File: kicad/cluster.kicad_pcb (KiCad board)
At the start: 2 copper layers, 24.5 x 36.5 mm, 17 parts, among them J1 Conn_01x07

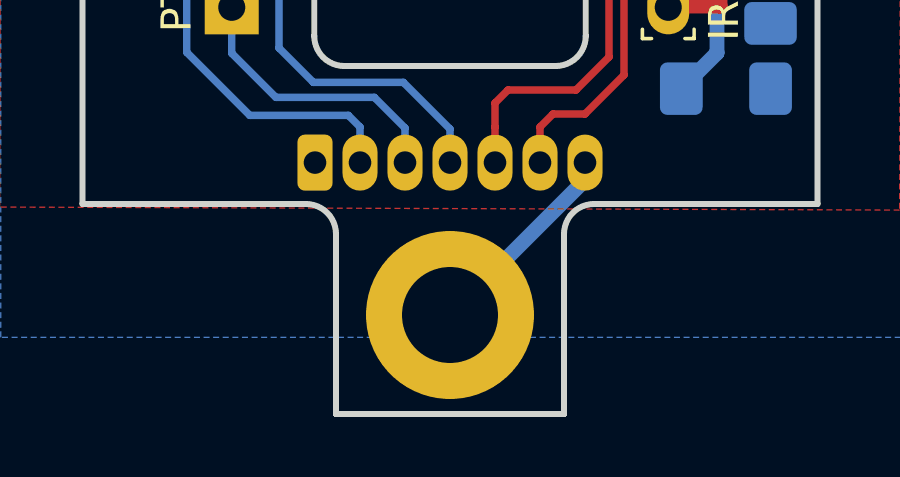
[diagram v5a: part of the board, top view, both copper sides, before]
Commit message: Update the various sensitivity-related resistor values
This updates the transimpedance amplifier resistors to 2k, and adjusts
the LED drive resistors to an appropriate level, from empirical testing.
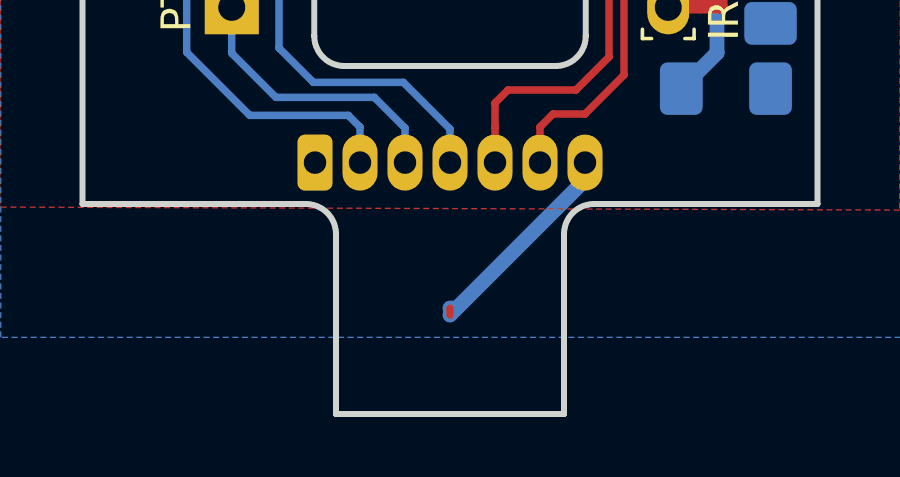
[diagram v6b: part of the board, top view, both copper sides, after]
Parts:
- removed REF**: MountingHole_3.2mm_M3, MountingHole:MountingHole_3.2mm_M3_DIN965_Pad
- R1, R2, R3, R4, R5: value 150 -> 270
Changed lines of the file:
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@@
     (tracks 76)
     (zones 0)
-    (modules 17)
+    (modules 16)
     (nets 13)
   )
@@
   (layers
     (0 F.Cu signal)
-    (31 B.Cu signal)
+    (31 B.Cu signal hide)
     (34 B.Paste user hide)
-    (35 F.Paste user hide)
-    (36 B.SilkS user)
+    (35 F.Paste user)
+    (36 B.SilkS user hide)
     (37 F.SilkS user)
     (38 B.Mask user hide)
-    (39 F.Mask user hide)
-    (40 Dwgs.User user)
+    (39 F.Mask user)
+    (40 Dwgs.User user hide)
     (44 Edge.Cuts user)
     (45 Margin user hide)
     (46 B.CrtYd user hide)
-    (47 F.CrtYd user hide)
-    (48 B.Fab user)
+    (47 F.CrtYd user)
+    (48 B.Fab user hide)
     (49 F.Fab user)
   )
@@
       (effects (font (size 1 1) (thickness 0.15)) (justify mirror))
     )
-    (fp_text value 150 (at 0 -1.82) (layer B.Fab)
+    (fp_text value 270 (at -3.9475 0.035) (layer B.SilkS)
       (effects (font (size 1 1) (thickness 0.15)) (justify mirror))
     )
@@
     )
   )
-  (module MountingHole:MountingHole_3.2mm_M3_DIN965_Pad (layer F.Cu)
-    (at 162.45 96.5)
-    (descr "Mounting Hole 3.2mm, M3, DIN965")
-    (tags "mounting hole 3.2mm m3 din965")
-    (attr virtual)
-    (fp_text reference REF** (at 0 -3.8) (layer F.SilkS) hide
-      (effects (font (size 1 1) (thickness 0.15)))
-    )
-    (fp_text value MountingHole_3.2mm_M3 (at 0 4.2) (layer F.Fab)
-      (effects (font (size 1 1) (thickness 0.15)))
-    )
-    (fp_circle (center 0 0) (end 2.8 0) (layer Cmts.User) (width 0.15))
-    (fp_circle (center 0 0) (end 3.05 0) (layer F.CrtYd) (width 0.05))
-    (pad 1 thru_hole circle (at 0 0) (size 5.6 5.6) (drill 3.2) (layers *.Cu *.Mask)
-      (net 12 GND))
-  )
   (module lalboard:IR908-7C-F (layer F.Cu)
     (at 156.425 67.395 90)
@@
       (effects (font (size 1 1) (thickness 0.15)) (justify mirror))
     )
-    (fp_text value 150 (at 0 -1.82 270) (layer B.Fab)
-      (effects (font (size 1 1) (thickness 0.15)) (justify mirror))
+    (fp_text value 270 (at 0 1.655 270) (layer B.SilkS)
+      (effects (font (size 0.75 0.75) (thickness 0.125)) (justify mirror))
     )
     (fp_line (start -1.6 -0.8) (end -1.6 0.8) (layer B.Fab) (width 0.1))
@@
       (effects (font (size 1 1) (thickness 0.15)) (justify mirror))
     )
-    (fp_text value 150 (at 0 -1.82 270) (layer B.Fab)
-      (effects (font (size 1 1) (thickness 0.15)) (justify mirror))
+    (fp_text value 270 (at 0 -1.649999 270) (layer B.SilkS)
+      (effects (font (size 0.75 0.75) (thickness 0.125)) (justify mirror))
     )
     (fp_line (start -1.6 -0.8) (end -1.6 0.8) (layer B.Fab) (width 0.1))
@@
       (effects (font (size 1 1) (thickness 0.15)) (justify mirror))
     )
-    (fp_text value 150 (at 0 -1.82 180) (layer B.Fab)
+    (fp_text value 270 (at 0 -1.82 180) (layer B.SilkS)
       (effects (font (size 1 1) (thickness 0.15)) (justify mirror))
     )
@@
       (effects (font (size 1 1) (thickness 0.15)) (justify mirror))
     )
-    (fp_text value 150 (at 0 -1.82 270) (layer B.Fab)
+    (fp_text value 270 (at 0 -1.735 270) (layer B.SilkS)
       (effects (font (size 1 1) (thickness 0.15)) (justify mirror))
     )
@@
   (segment (start 170.275 81.245) (end 170.605 81.575) (width 0.5) (layer F.Cu) (net 1))
   (via (at 164.875008 81.245) (size 0.8) (drill 0.4) (layers F.Cu B.Cu) (net 1))
+  (segment (start 157.849999 71.22) (end 157.849999 73.3) (width 0.35) (layer B.Cu) (net 2))
+  (segment (start 154.829999 68.2) (end 157.849999 71.22) (width 0.35) (layer B.Cu) (net 2))
+  (segment (start 153.08 68.2) (end 154.829999 68.2) (width 0.35) (layer B.Cu) (net 2))
+  (segment (start 151.755 69.525) (end 153.08 68.2) (width 0.35) (layer B.Cu) (net 2))
+  (segment (start 171.35 84.400001) (end 171.35 87.765) (width 0.5) (layer B.Cu) (net 3))
+  (segment (start 169.725 83.705) (end 170.654999 83.705) (width 0.5) (layer B.Cu) (net 3))
+  (segment (start 170.654999 83.705) (end 171.35 84.400001) (width 0.5) (layer B.Cu) (net 3))
+  (segment (start 171.35 87.765) (end 170.16 88.955) (width 0.5) (layer B.Cu) (net 3))
+  (segment (start 167.855 78.085) (end 168.475 78.705) (width 0.25) (layer B.Cu) (net 4))
+  (segment (start 167.855 76.3825) (end 167.855 78.085) (width 0.5) (layer B.Cu) (net 4))
+  (segment (start 156.425 67.395) (end 158.965 69.935) (width 0.5) (layer B.Cu) (net 5))
+  (segment (start 173.135 81.585) (end 173.145 81.575) (width 0.25) (layer B.Cu) (net 6))
+  (segment (start 173.135 83.805) (end 173.135 81.585) (width 0.5) (layer B.Cu) (net 6))
   (segment (start 154.295 81.575) (end 153.675 82.195) (width 0.25) (layer B.Cu) (net 7))
   (segment (start 155.775 89.845) (end 159.06 89.845) (width 0.25) (layer B.Cu) (net 7))
@@
   (segment (start 153.675 87.745) (end 155.775 89.845) (width 0.25) (layer B.Cu) (net 7))
   (segment (start 153.739999 82.130001) (end 154.295 81.575) (width 0.25) (layer F.Cu) (net 7))
-  (segment (start 157.895 88.745) (end 160.895 88.745) (width 0.25) (layer B.Cu) (net 10))
-  (segment (start 156.425 81.975) (end 156.75 82.3) (width 0.25) (layer B.Cu) (net 10))
-  (segment (start 156.75 82.3) (end 156.75 87.6) (width 0.25) (layer B.Cu) (net 10))
-  (segment (start 156.425 81.245) (end 156.425 81.975) (width 0.25) (layer F.Cu) (net 10))
-  (segment (start 162.45 90.3) (end 162.45 91.42) (width 0.25) (layer B.Cu) (net 10))
-  (segment (start 160.895 88.745) (end 162.45 90.3) (width 0.25) (layer B.Cu) (net 10))
-  (segment (start 156.75 87.6) (end 157.895 88.745) (width 0.25) (layer B.Cu) (net 10))
+  (segment (start 156.645 89.245) (end 159.9275 89.245) (width 0.25) (layer B.Cu) (net 8))
+  (segment (start 155.175 86.245) (end 155.175 87.775) (width 0.25) (layer B.Cu) (net 8))
+  (segment (start 160.95 90.2675) (end 160.95 91.42) (width 0.25) (layer B.Cu) (net 8))
+  (segment (start 155.175 87.775) (end 156.645 89.245) (width 0.25) (layer B.Cu) (net 8))
+  (segment (start 159.9275 89.245) (end 160.95 90.2675) (width 0.25) (layer B.Cu) (net 8))
   (segment (start 166.65 89) (end 164.384998 89) (width 0.25) (layer F.Cu) (net 9))
   (segment (start 166.25 71.47) (end 166.25 80.426998) (width 0.25) (layer F.Cu) (net 9))
@@
   (segment (start 167.75 87.9) (end 166.65 89) (width 0.25) (layer F.Cu) (net 9))
   (segment (start 167.75 83.5) (end 167.75 87.9) (width 0.25) (layer F.Cu) (net 9))
+  (segment (start 157.895 88.745) (end 160.895 88.745) (width 0.25) (layer B.Cu) (net 10))
+  (segment (start 156.425 81.975) (end 156.75 82.3) (width 0.25) (layer B.Cu) (net 10))
+  (segment (start 156.75 82.3) (end 156.75 87.6) (width 0.25) (layer B.Cu) (net 10))
+  (segment (start 156.425 81.245) (end 156.425 81.975) (width 0.25) (layer F.Cu) (net 10))
+  (segment (start 162.45 90.3) (end 162.45 91.42) (width 0.25) (layer B.Cu) (net 10))
+  (segment (start 160.895 88.745) (end 162.45 90.3) (width 0.25) (layer B.Cu) (net 10))
+  (segment (start 156.75 87.6) (end 157.895 88.745) (width 0.25) (layer B.Cu) (net 10))
   (segment (start 168.25 83.25) (end 168.25 88.5) (width 0.25) (layer F.Cu) (net 11))
   (segment (start 170.605 69.525) (end 169.455 69.525) (width 0.25) (layer F.Cu) (net 11))
@@
   (segment (start 162.45 96.27) (end 162.45 96.5) (width 0.25) (layer F.Cu) (net 12))
   (segment (start 166.95 91.77) (end 166.95 91.87) (width 0.5) (layer B.Cu) (net 12))
-  (segment (start 157.849999 71.22) (end 157.849999 73.3) (width 0.35) (layer B.Cu) (net 2))
-  (segment (start 154.829999 68.2) (end 157.849999 71.22) (width 0.35) (layer B.Cu) (net 2))
-  (segment (start 153.08 68.2) (end 154.829999 68.2) (width 0.35) (layer B.Cu) (net 2))
-  (segment (start 151.755 69.525) (end 153.08 68.2) (width 0.35) (layer B.Cu) (net 2))
-  (segment (start 171.35 84.400001) (end 171.35 87.765) (width 0.5) (layer B.Cu) (net 3))
-  (segment (start 169.725 83.705) (end 170.654999 83.705) (width 0.5) (layer B.Cu) (net 3))
-  (segment (start 170.654999 83.705) (end 171.35 84.400001) (width 0.5) (layer B.Cu) (net 3))
-  (segment (start 171.35 87.765) (end 170.16 88.955) (width 0.5) (layer B.Cu) (net 3))
-  (segment (start 167.855 78.085) (end 168.475 78.705) (width 0.25) (layer B.Cu) (net 4))
-  (segment (start 167.855 76.3825) (end 167.855 78.085) (width 0.5) (layer B.Cu) (net 4))
-  (segment (start 156.425 67.395) (end 158.965 69.935) (width 0.5) (layer B.Cu) (net 5))
-  (segment (start 173.135 81.585) (end 173.145 81.575) (width 0.25) (layer B.Cu) (net 6))
-  (segment (start 173.135 83.805) (end 173.135 81.585) (width 0.5) (layer B.Cu) (net 6))
-  (segment (start 156.645 89.245) (end 159.9275 89.245) (width 0.25) (layer B.Cu) (net 8))
-  (segment (start 155.175 86.245) (end 155.175 87.775) (width 0.25) (layer B.Cu) (net 8))
-  (segment (start 160.95 90.2675) (end 160.95 91.42) (width 0.25) (layer B.Cu) (net 8))
-  (segment (start 155.175 87.775) (end 156.645 89.245) (width 0.25) (layer B.Cu) (net 8))
-  (segment (start 159.9275 89.245) (end 160.95 90.2675) (width 0.25) (layer B.Cu) (net 8))
   (segment (start 166.95 92) (end 162.45 96.5) (width 0.5) (layer B.Cu) (net 12))
   (segment (start 166.95 91.42) (end 166.95 92) (width 0.25) (layer B.Cu) (net 12))

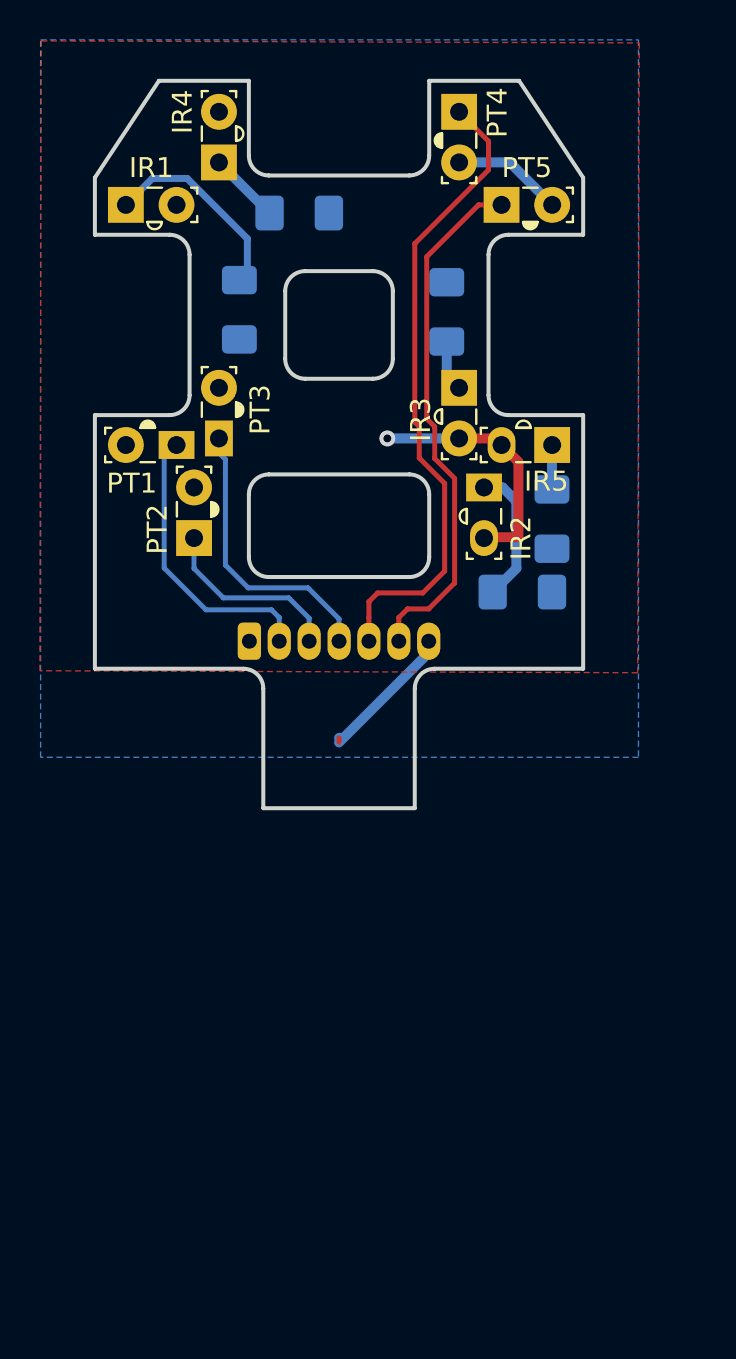
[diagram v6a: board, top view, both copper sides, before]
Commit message: Update cluster pcb for v2.5
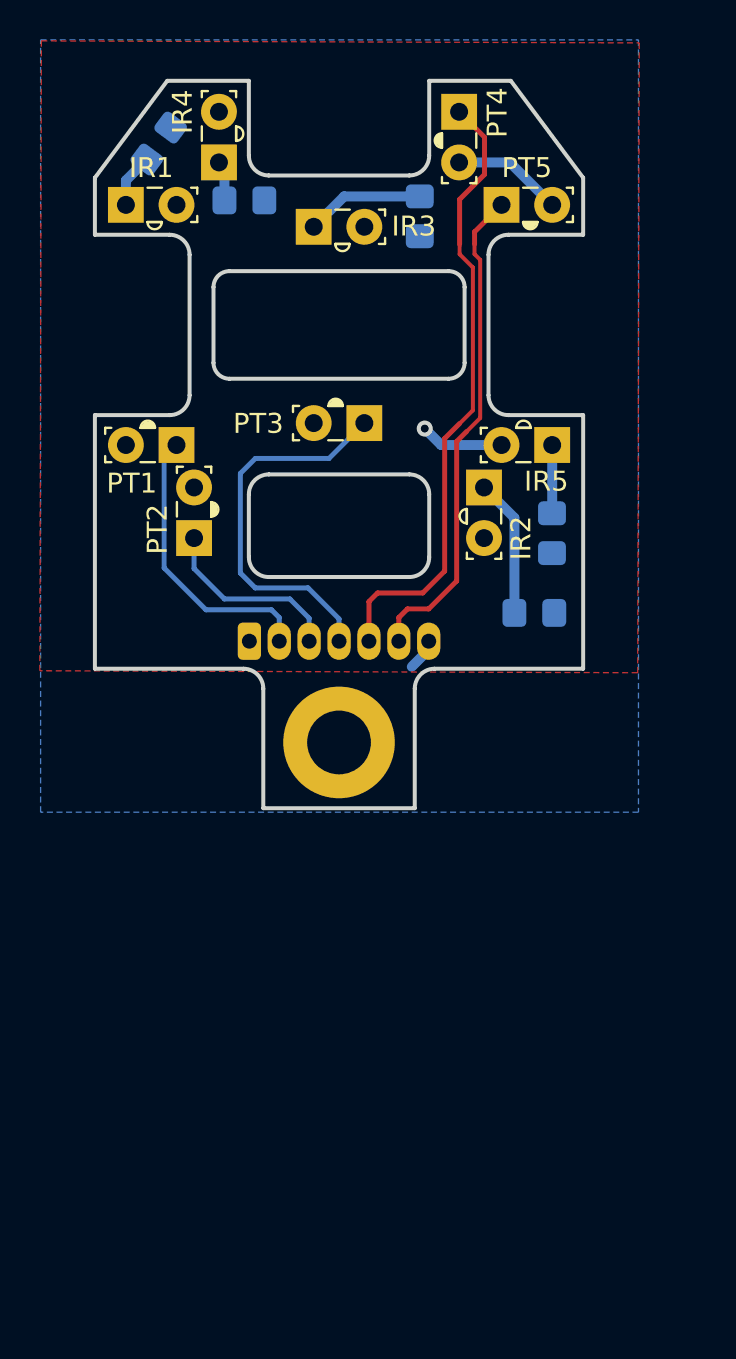
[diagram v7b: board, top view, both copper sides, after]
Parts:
- added H1: MountingHole_Pad, MountingHole:MountingHole_3.2mm_M3_DIN965_Pad, F.Cu at (162.4, 96.5)
- R1, R2, R3, R4, R5: footprint Resistor_SMD:R_1206_3216Metric_Pad1.42x1.75mm_HandSolder -> Resistor_SMD:R_0805_2012Metric_Pad1.20x1.40mm_HandSolder
- moved IR3 10.9 mm to (161.2, 70.6), turned to 0 degrees
- moved R1 9.27 mm to (153.4, 66.4), turned to -126.7 degrees
- moved PT3 7.34 mm to (163.7, 80.5), turned to 180 degrees
- moved R3 4.98 mm to (166.5, 70.1), turned to 90 degrees
- moved R4 2.82 mm to (157.7, 69.3)
- moved R2 1.21 mm to (172.2, 90.0)
- moved R5 0.71 mm to (173.1, 86.0)
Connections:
- net +5V renamed +3.3V
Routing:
- net +3.3V: track 18.4 -> 10.1 mm
- net Net-(IR1-K): track 9.97 -> 2.71 mm
- net GND: track 7.76 -> 2.31 mm
- net C3: track 14.4 -> 19.3 mm
- net Net-(IR3-K): track 2.58 -> 5.95 mm
- net C5: track 26.5 -> 24.9 mm
- net Net-(IR5-K): track 2.23 -> 3.43 mm
- net C4: track 32.2 -> 31.4 mm
- net C1: track 15.2 -> 14.4 mm
- net Net-(IR4-K): track 3.59 -> 2.83 mm
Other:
- outline, holes or cut-outs redrawn
- net class Default removed
- net class Power removed
- board text added: "lalboard.com finger cluster"
- board text added: "v2.5.0"
- board text removed: "Min internal corner radius: .8mm (for all internal corners)"
- board text removed: "finger cluster v0.1"
- board text removed: "lalboard.com"

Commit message: Add production files for the PCBs
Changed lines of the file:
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@@
     (grid_origin 150 100)
     (pcbplotparams
-      (layerselection 0x00210f0_ffffffff)
+      (layerselection 0x00010f0_ffffffff)
       (plot_on_all_layers_selection 0x0000000_00000000)
       (disableapertmacros false)
-      (usegerberextensions false)
-      (usegerberattributes true)
-      (usegerberadvancedattributes true)
-      (creategerberjobfile true)
+      (usegerberextensions true)
+      (usegerberattributes false)
+      (usegerberadvancedattributes false)
+      (creategerberjobfile false)
       (dashed_line_dash_ratio 12.000000)
       (dashed_line_gap_ratio 3.000000)
@@
       (psa4output false)
       (plotreference true)
-      (plotvalue true)
+      (plotvalue false)
       (plotinvisibletext false)
       (sketchpadsonfab false)
-      (subtractmaskfromsilk false)
+      (subtractmaskfromsilk true)
       (outputformat 1)
       (mirror false)
       (drillshape 0)
       (scaleselection 1)
-      (outputdirectory "/tmp/cluster/")
+      (outputdirectory "/home/jesusfreke/projects/lalboard/kicad/production_files/cluster")
     )
   )
@@
     (fp_line (start 1 0.625) (end 1 -0.625)
       (stroke (width 0.1) (type solid)) (layer "B.Fab"))
-    (pad "1" smd roundrect (at -1 0 90) (size 1.2 1.4) (layers "B.Cu" "B.Paste" "B.Mask") (roundrect_rratio 0.208333)
+    (pad "1" smd roundrect (at -1 0 90) (size 1.2 1.4) (layers "B.Cu" "B.Paste" "B.Mask") (roundrect_rratio 0.2083333333)
       (net 12 "GND") (pintype "passive"))
-    (pad "2" smd roundrect (at 1 0 90) (size 1.2 1.4) (layers "B.Cu" "B.Paste" "B.Mask") (roundrect_rratio 0.208333)
+    (pad "2" smd roundrect (at 1 0 90) (size 1.2 1.4) (layers "B.Cu" "B.Paste" "B.Mask") (roundrect_rratio 0.2083333333)
       (net 6 "Net-(IR5-K)") (pintype "passive"))
     (model "${KICAD6_3DMODEL_DIR}/Resistor_SMD.3dshapes/R_0805_2012Metric.wrl"
@@
     (fp_line (start 1 0.625) (end 1 -0.625)
       (stroke (width 0.1) (type solid)) (layer "B.Fab"))
-    (pad "1" smd roundrect (at -1 0 180) (size 1.2 1.4) (layers "B.Cu" "B.Paste" "B.Mask") (roundrect_rratio 0.208333)
+    (pad "1" smd roundrect (at -1 0 180) (size 1.2 1.4) (layers "B.Cu" "B.Paste" "B.Mask") (roundrect_rratio 0.2083333333)
       (net 12 "GND") (pintype "passive"))
-    (pad "2" smd roundrect (at 1 0 180) (size 1.2 1.4) (layers "B.Cu" "B.Paste" "B.Mask") (roundrect_rratio 0.208333)
+    (pad "2" smd roundrect (at 1 0 180) (size 1.2 1.4) (layers "B.Cu" "B.Paste" "B.Mask") (roundrect_rratio 0.2083333333)
       (net 3 "Net-(IR2-K)") (pintype "passive"))
     (model "${KICAD6_3DMODEL_DIR}/Resistor_SMD.3dshapes/R_0805_2012Metric.wrl"
@@
     (fp_line (start 1 0.625) (end 1 -0.625)
       (stroke (width 0.1) (type solid)) (layer "B.Fab"))
-    (pad "1" smd roundrect (at -1 0 233.3) (size 1.2 1.4) (layers "B.Cu" "B.Paste" "B.Mask") (roundrect_rratio 0.208333)
+    (pad "1" smd roundrect (at -1 0 233.3) (size 1.2 1.4) (layers "B.Cu" "B.Paste" "B.Mask") (roundrect_rratio 0.2083333333)
       (net 12 "GND") (pintype "passive") (zone_connect 1))
-    (pad "2" smd roundrect (at 1 0 233.3) (size 1.2 1.4) (layers "B.Cu" "B.Paste" "B.Mask") (roundrect_rratio 0.208333)
+    (pad "2" smd roundrect (at 1 0 233.3) (size 1.2 1.4) (layers "B.Cu" "B.Paste" "B.Mask") (roundrect_rratio 0.2083333333)
       (net 1 "Net-(IR1-K)") (pintype "passive"))
     (model "${KICAD6_3DMODEL_DIR}/Resistor_SMD.3dshapes/R_0805_2012Metric.wrl"
@@
     (fp_line (start 1 0.625) (end 1 -0.625)
       (stroke (width 0.1) (type solid)) (layer "B.Fab"))
-    (pad "1" smd roundrect (at -1 0 180) (size 1.2 1.4) (layers "B.Cu" "B.Paste" "B.Mask") (roundrect_rratio 0.208333)
+    (pad "1" smd roundrect (at -1 0 180) (size 1.2 1.4) (layers "B.Cu" "B.Paste" "B.Mask") (roundrect_rratio 0.2083333333)
       (net 12 "GND") (pintype "passive") (zone_connect 1))
-    (pad "2" smd roundrect (at 1 0 180) (size 1.2 1.4) (layers "B.Cu" "B.Paste" "B.Mask") (roundrect_rratio 0.208333)
+    (pad "2" smd roundrect (at 1 0 180) (size 1.2 1.4) (layers "B.Cu" "B.Paste" "B.Mask") (roundrect_rratio 0.2083333333)
       (net 5 "Net-(IR4-K)") (pintype "passive"))
     (model "${KICAD6_3DMODEL_DIR}/Resistor_SMD.3dshapes/R_0805_2012Metric.wrl"
@@
     (fp_line (start 1 0.625) (end 1 -0.625)
       (stroke (width 0.1) (type solid)) (layer "B.Fab"))
-    (pad "1" smd roundrect (at -1 0 90) (size 1.2 1.4) (layers "B.Cu" "B.Paste" "B.Mask") (roundrect_rratio 0.208333)
+    (pad "1" smd roundrect (at -1 0 90) (size 1.2 1.4) (layers "B.Cu" "B.Paste" "B.Mask") (roundrect_rratio 0.2083333333)
       (net 12 "GND") (pintype "passive") (zone_connect 1))
-    (pad "2" smd roundrect (at 1 0 90) (size 1.2 1.4) (layers "B.Cu" "B.Paste" "B.Mask") (roundrect_rratio 0.208333)
+    (pad "2" smd roundrect (at 1 0 90) (size 1.2 1.4) (layers "B.Cu" "B.Paste" "B.Mask") (roundrect_rratio 0.2083333333)
       (net 4 "Net-(IR3-K)") (pintype "passive"))
     (model "${KICAD6_3DMODEL_DIR}/Resistor_SMD.3dshapes/R_0805_2012Metric.wrl"
